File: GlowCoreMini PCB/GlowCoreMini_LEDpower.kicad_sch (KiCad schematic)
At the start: 12 parts, among them U1 SN74LVC1G373DBVR, U4 AP40P05, U5 AP40P05, U6 AO3400A

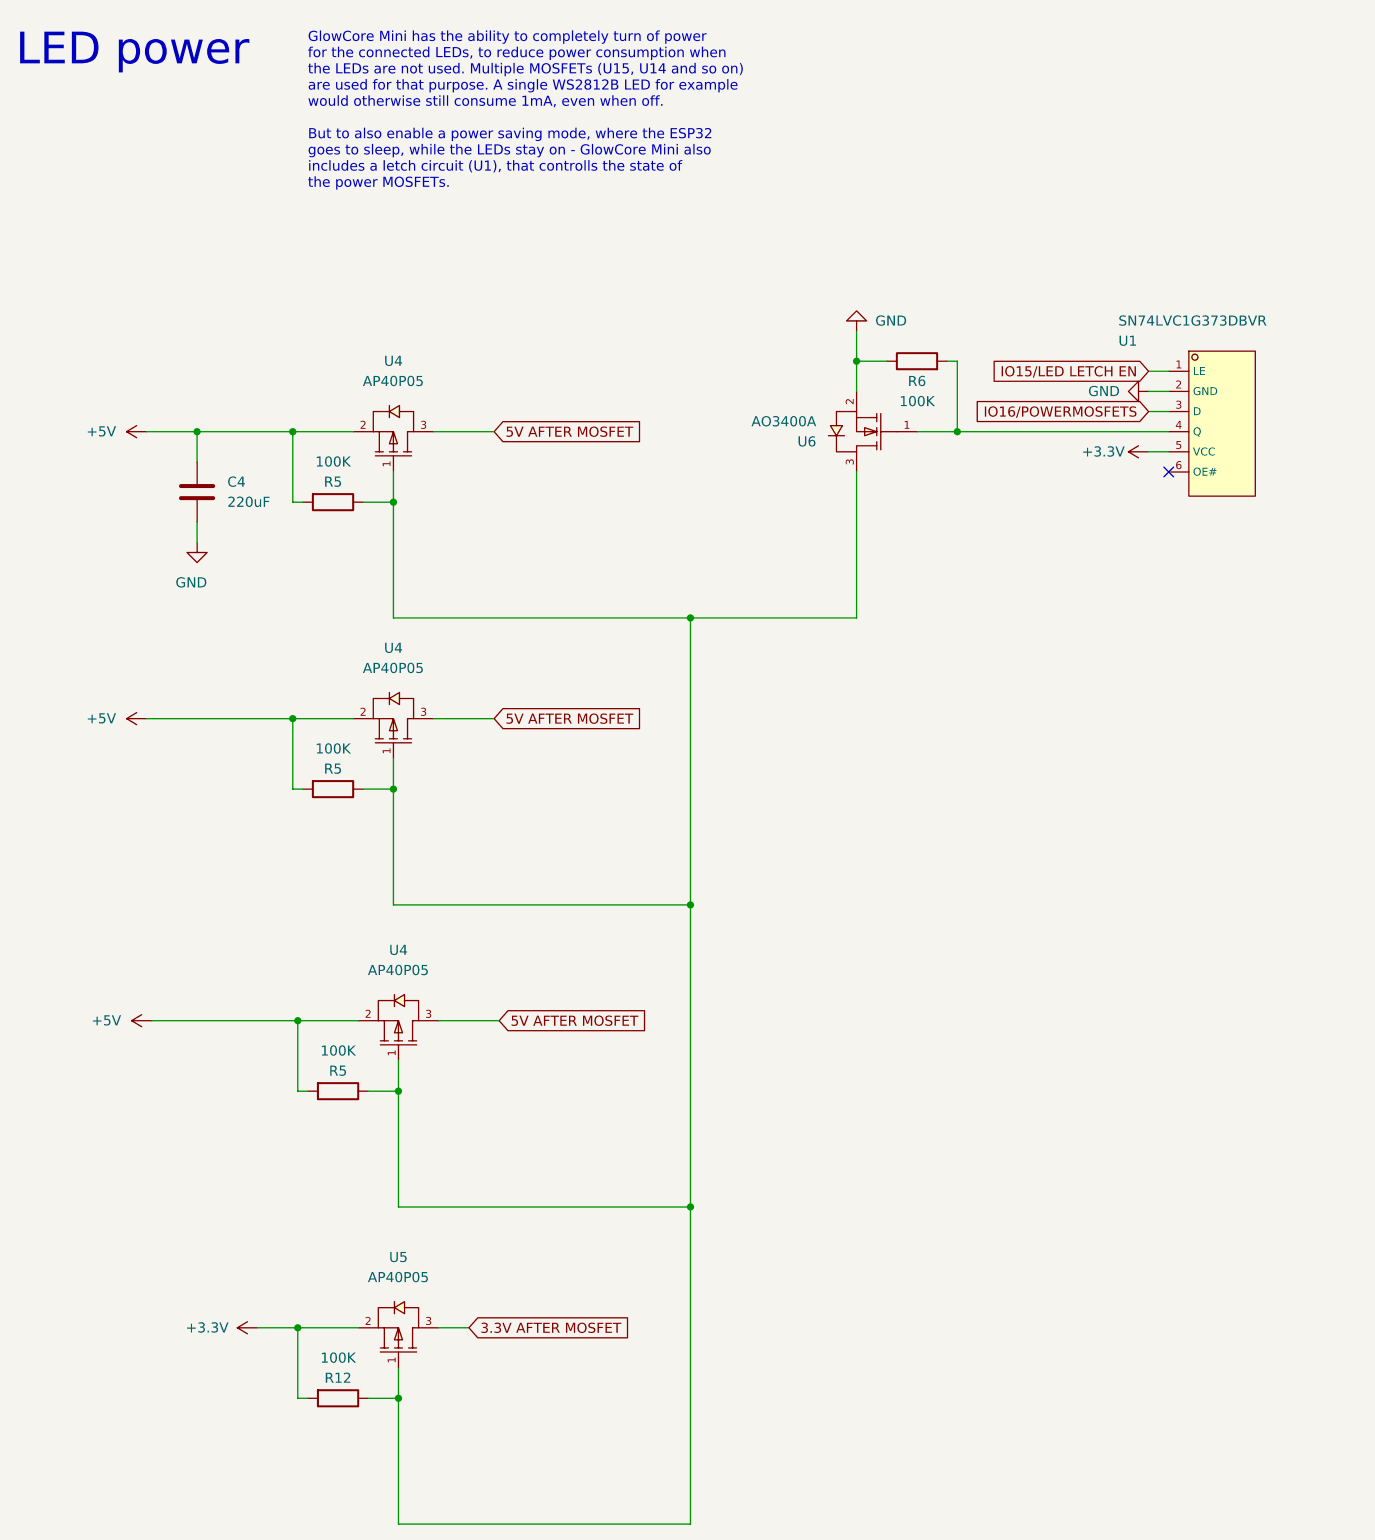
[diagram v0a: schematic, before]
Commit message: split up schematic
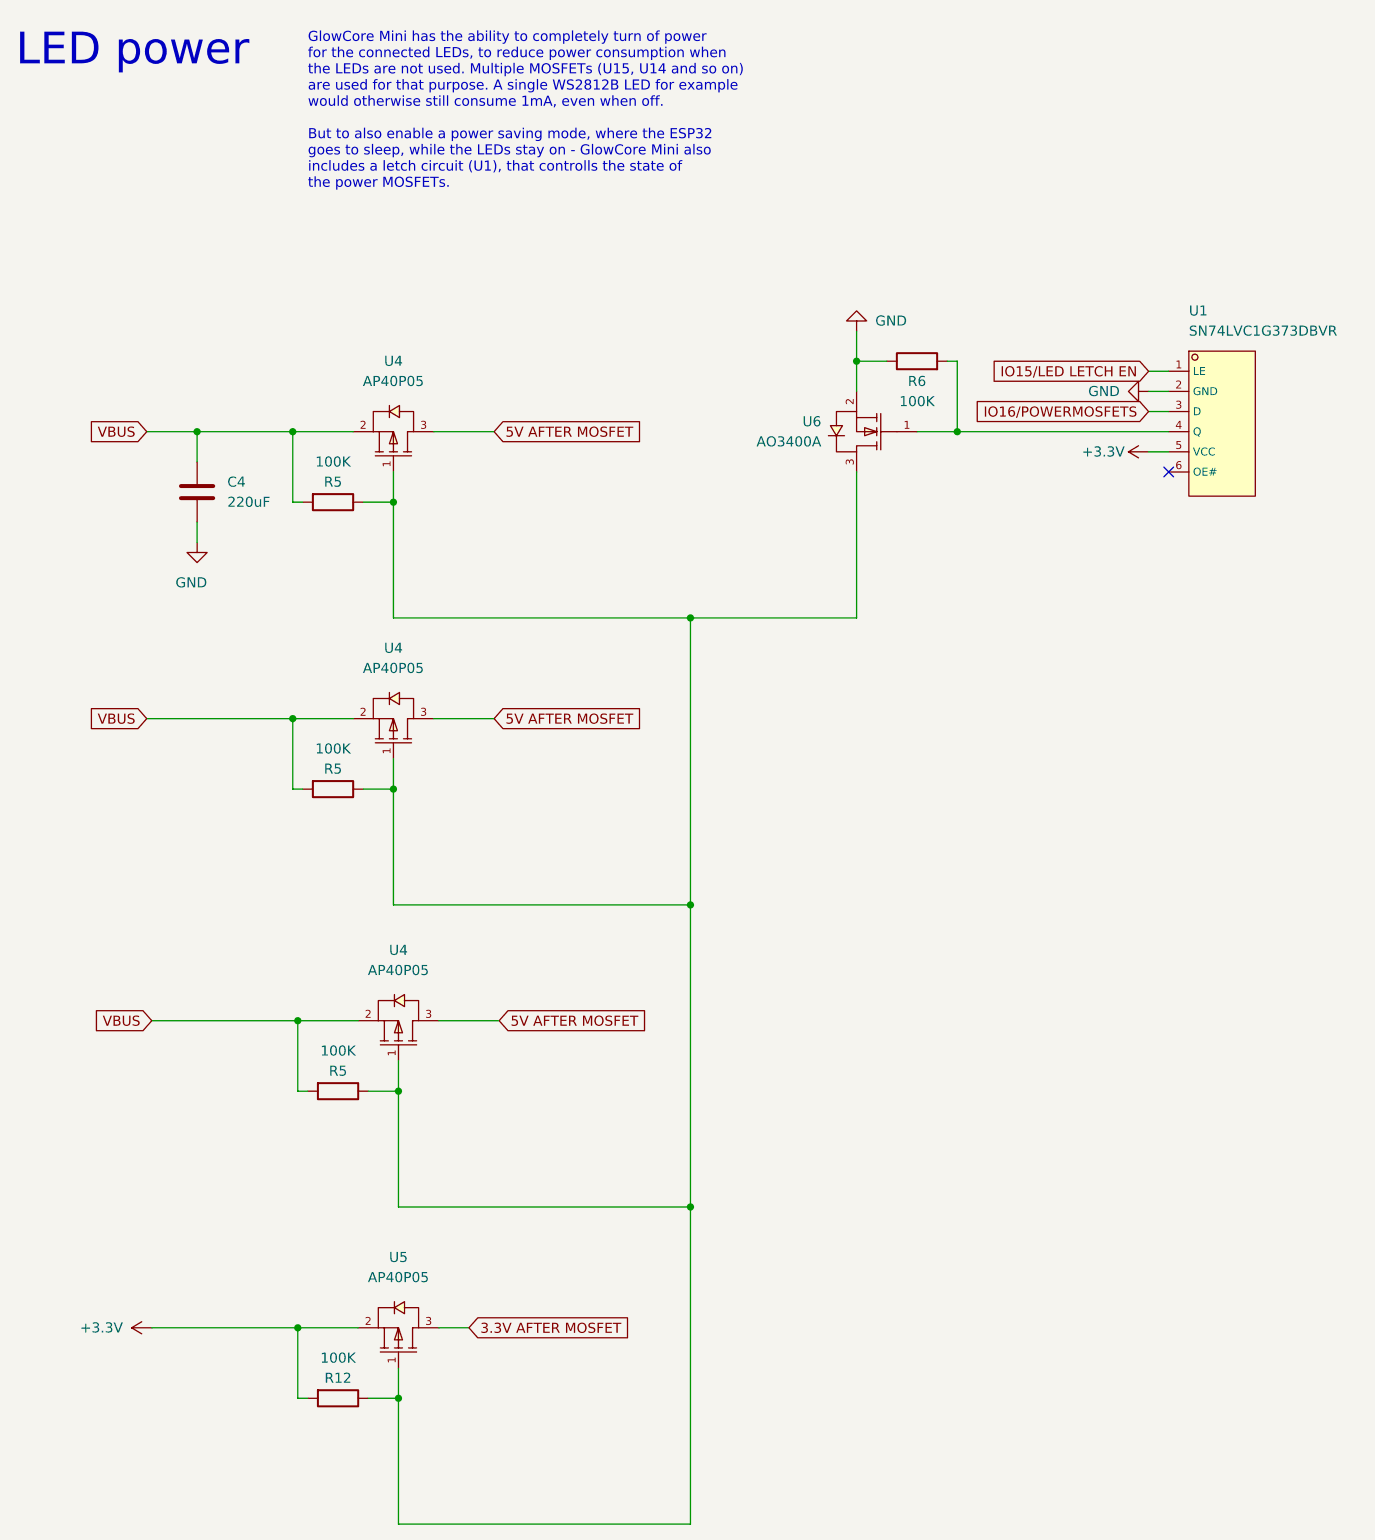
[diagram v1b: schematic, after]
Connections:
- net +5V renamed VBUS
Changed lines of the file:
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@@
     (stroke (width 0) (type default))
   )
-  (wire (pts (xy 49.53 184.15) (xy 54.61 184.15))
+  (wire (pts (xy 36.195 184.15) (xy 54.61 184.15))
     (stroke (width 0) (type default))
   )
@@
     (property "Intersheetrefs" "${INTERSHEET_REFS}" (at 95.8488 184.0706 0)
       (effects (font (size 1.27 1.27)) (justify left) hide)
+    )
+  )
+  (global_label "VBUS" (shape input) (at 35.56 107.315 180) (fields_autoplaced)
+    (effects (font (size 1.27 1.27)) (justify right))
+    (property "Intersheetrefs" "${INTERSHEET_REFS}" (at 27.9099 107.315 0)
+      (effects (font (size 1.27 1.27)) (justify right) hide)
     )
   )
@@
     )
   )
+  (global_label "VBUS" (shape input) (at 36.195 145.415 180) (fields_autoplaced)
+    (effects (font (size 1.27 1.27)) (justify right))
+    (property "Intersheetrefs" "${INTERSHEET_REFS}" (at 28.5449 145.415 0)
+      (effects (font (size 1.27 1.27)) (justify right) hide)
+    )
+  )
   (global_label "5V AFTER MOSFET" (shape input) (at 80.01 145.415 0) (fields_autoplaced)
     (effects (font (size 1.27 1.27)) (justify left))
@@
     )
   )
+  (global_label "VBUS" (shape input) (at 35.56 71.12 180) (fields_autoplaced)
+    (effects (font (size 1.27 1.27)) (justify right))
+    (property "Intersheetrefs" "${INTERSHEET_REFS}" (at 27.9099 71.12 0)
+      (effects (font (size 1.27 1.27)) (justify right) hide)
+    )
+  )
   (symbol (lib_id "power:GND") (at 125.095 58.42 180) (unit 1)
     (in_bom yes) (on_board yes) (dnp no)
@@
         (path "/c6f71574-e06f-4ae6-b347-b6a4861b944a/c8067d67-dedb-425c-9ffb-c9d76922c7bd"
           (reference "R22") (unit 1)
-        )
-      )
-    )
-  )
-  (symbol (lib_id "power:+5V") (at 35.56 71.12 90) (unit 1)
-    (in_bom yes) (on_board yes) (dnp no)
-    (property "Reference" "#PWR0137" (at 39.37 71.12 0)
-      (effects (font (size 1.27 1.27)) hide)
-    )
-    (property "Value" "+5V" (at 27.94 71.12 90)
-      (effects (font (size 1.27 1.27)) (justify right))
-    )
-    (property "Footprint" "" (at 35.56 71.12 0)
-      (effects (font (size 1.27 1.27)) hide)
-    )
-    (property "Datasheet" "" (at 35.56 71.12 0)
-      (effects (font (size 1.27 1.27)) hide)
-    )
-    (pin "1")
-    (instances
-      (project "GlowCoreMini PCB"
-        (path "/c6f71574-e06f-4ae6-b347-b6a4861b944a"
-          (reference "#PWR0137") (unit 1)
-        )
-        (path "/c6f71574-e06f-4ae6-b347-b6a4861b944a/c8067d67-dedb-425c-9ffb-c9d76922c7bd"
-          (reference "#PWR0161") (unit 1)
         )
       )
@@
     )
   )
-  (symbol (lib_id "power:+3.3V") (at 49.53 184.15 90) (unit 1)
-    (in_bom yes) (on_board yes) (dnp no)
-    (property "Reference" "#PWR0141" (at 53.34 184.15 0)
-      (effects (font (size 1.27 1.27)) hide)
-    )
-    (property "Value" "+3.3V" (at 43.18 184.15 90)
-      (effects (font (size 1.27 1.27)))
-    )
-    (property "Footprint" "" (at 49.53 184.15 0)
-      (effects (font (size 1.27 1.27)) hide)
-    )
-    (property "Datasheet" "" (at 49.53 184.15 0)
+  (symbol (lib_id "power:+3.3V") (at 36.195 184.15 90) (unit 1)
+    (in_bom yes) (on_board yes) (dnp no)
+    (property "Reference" "#PWR0141" (at 40.005 184.15 0)
+      (effects (font (size 1.27 1.27)) hide)
+    )
+    (property "Value" "+3.3V" (at 29.845 184.15 90)
+      (effects (font (size 1.27 1.27)))
+    )
+    (property "Footprint" "" (at 36.195 184.15 0)
+      (effects (font (size 1.27 1.27)) hide)
+    )
+    (property "Datasheet" "" (at 36.195 184.15 0)
       (effects (font (size 1.27 1.27)) hide)
     )
@@
   )
   (symbol (lib_id "MyParts:AO3400A") (at 23.495 7.62 180) (unit 1)
-    (in_bom yes) (on_board yes) (dnp no) (fields_autoplaced)
-    (property "Reference" "U6" (at 120.015 72.3901 0)
-      (effects (font (size 1.27 1.27)) (justify left))
-    )
-    (property "Value" "AO3400A" (at 120.015 69.8501 0)
+    (in_bom yes) (on_board yes) (dnp no)
+    (property "Reference" "U6" (at 120.65 69.85 0)
+      (effects (font (size 1.27 1.27)) (justify left))
+    )
+    (property "Value" "AO3400A" (at 120.65 72.39 0)
       (effects (font (size 1.27 1.27)) (justify left))
     )
@@
   (symbol (lib_id "MyParts:SN74LVC1G373DBVR") (at 167.005 50.8 0) (unit 1)
     (in_bom yes) (on_board yes) (dnp no)
-    (property "Reference" "U1" (at 158.115 59.69 0)
-      (effects (font (size 1.27 1.27)) (justify left))
-    )
-    (property "Value" "SN74LVC1G373DBVR" (at 158.115 57.15 0)
+    (property "Reference" "U1" (at 167.005 55.88 0)
+      (effects (font (size 1.27 1.27)) (justify left))
+    )
+    (property "Value" "SN74LVC1G373DBVR" (at 167.005 58.42 0)
       (effects (font (size 1.27 1.27)) (justify left))
     )
@@
     )
   )
-  (symbol (lib_id "power:+5V") (at 35.56 107.315 90) (unit 1)
-    (in_bom yes) (on_board yes) (dnp no)
-    (property "Reference" "#PWR0137" (at 39.37 107.315 0)
-      (effects (font (size 1.27 1.27)) hide)
-    )
-    (property "Value" "+5V" (at 27.94 107.315 90)
-      (effects (font (size 1.27 1.27)) (justify right))
-    )
-    (property "Footprint" "" (at 35.56 107.315 0)
-      (effects (font (size 1.27 1.27)) hide)
-    )
-    (property "Datasheet" "" (at 35.56 107.315 0)
-      (effects (font (size 1.27 1.27)) hide)
-    )
-    (pin "1")
-    (instances
-      (project "GlowCoreMini PCB"
-        (path "/c6f71574-e06f-4ae6-b347-b6a4861b944a"
-          (reference "#PWR0137") (unit 1)
-        )
-        (path "/c6f71574-e06f-4ae6-b347-b6a4861b944a/c8067d67-dedb-425c-9ffb-c9d76922c7bd"
-          (reference "#PWR0159") (unit 1)
-        )
-      )
-    )
-  )
   (symbol (lib_id "MyParts:AP40P05") (at 68.58 145.415 270) (mirror x) (unit 1)
     (in_bom yes) (on_board yes) (dnp no) (fields_autoplaced)
@@
         )
       )
-    )
-  )
-  (symbol (lib_id "power:+5V") (at 36.195 145.415 90) (unit 1)
-    (in_bom yes) (on_board yes) (dnp no)
-    (property "Reference" "#PWR0137" (at 40.005 145.415 0)
-      (effects (font (size 1.27 1.27)) hide)
-    )
-    (property "Value" "+5V" (at 28.575 145.415 90)
-      (effects (font (size 1.27 1.27)) (justify right))
-    )
-    (property "Footprint" "" (at 36.195 145.415 0)
-      (effects (font (size 1.27 1.27)) hide)
-    )
-    (property "Datasheet" "" (at 36.195 145.415 0)
-      (effects (font (size 1.27 1.27)) hide)
-    )
-    (pin "1")
-    (instances
-      (project "GlowCoreMini PCB"
-        (path "/c6f71574-e06f-4ae6-b347-b6a4861b944a"
-          (reference "#PWR0137") (unit 1)
-        )
-        (path "/c6f71574-e06f-4ae6-b347-b6a4861b944a/c8067d67-dedb-425c-9ffb-c9d76922c7bd"
-          (reference "#PWR0137") (unit 1)
-        )
-      )
